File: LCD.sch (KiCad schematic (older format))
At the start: 11 parts

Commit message: Erste fertige Version
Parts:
- R? (x7): value 22 -> 220
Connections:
- net RW renamed R~W~
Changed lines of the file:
@@
 P 4500 3300
 F 0 "R?" V 4450 3150 50  0000 C CNN
-F 1 "22" V 4450 3450 50  0000 C CNN
+F 1 "220" V 4450 3450 50  0000 C CNN
 F 2 "" H 4500 3300 50  0001 C CNN
 F 3 "~" H 4500 3300 50  0001 C CNN
@@
 RS
 Text HLabel 4150 3400 0    50   Input ~ 0
-RW
+R~W~
 Text HLabel 4150 3500 0    50   Input ~ 0
 E
@@
 P 4500 3400
 F 0 "R?" V 4450 3250 50  0000 C CNN
-F 1 "22" V 4450 3550 50  0000 C CNN
+F 1 "220" V 4450 3550 50  0000 C CNN
 F 2 "" H 4500 3400 50  0001 C CNN
 F 3 "~" H 4500 3400 50  0001 C CNN
@@
 P 4500 3500
 F 0 "R?" V 4450 3350 50  0000 C CNN
-F 1 "22" V 4450 3650 50  0000 C CNN
+F 1 "220" V 4450 3650 50  0000 C CNN
 F 2 "" H 4500 3500 50  0001 C CNN
 F 3 "~" H 4500 3500 50  0001 C CNN
@@
 P 4500 4000
 F 0 "R?" V 4450 3850 50  0000 C CNN
-F 1 "22" V 4450 4150 50  0000 C CNN
+F 1 "220" V 4450 4150 50  0000 C CNN
 F 2 "" H 4500 4000 50  0001 C CNN
 F 3 "~" H 4500 4000 50  0001 C CNN
@@
 P 4500 4100
 F 0 "R?" V 4450 3950 50  0000 C CNN
-F 1 "22" V 4450 4250 50  0000 C CNN
+F 1 "220" V 4450 4250 50  0000 C CNN
 F 2 "" H 4500 4100 50  0001 C CNN
 F 3 "~" H 4500 4100 50  0001 C CNN
@@
 P 4500 4200
 F 0 "R?" V 4450 4050 50  0000 C CNN
-F 1 "22" V 4450 4350 50  0000 C CNN
+F 1 "220" V 4450 4350 50  0000 C CNN
 F 2 "" H 4500 4200 50  0001 C CNN
 F 3 "~" H 4500 4200 50  0001 C CNN
@@
 P 4500 4300
 F 0 "R?" V 4450 4150 50  0000 C CNN
-F 1 "22" V 4450 4450 50  0000 C CNN
+F 1 "220" V 4450 4450 50  0000 C CNN
 F 2 "" H 4500 4300 50  0001 C CNN
 F 3 "~" H 4500 4300 50  0001 C CNN

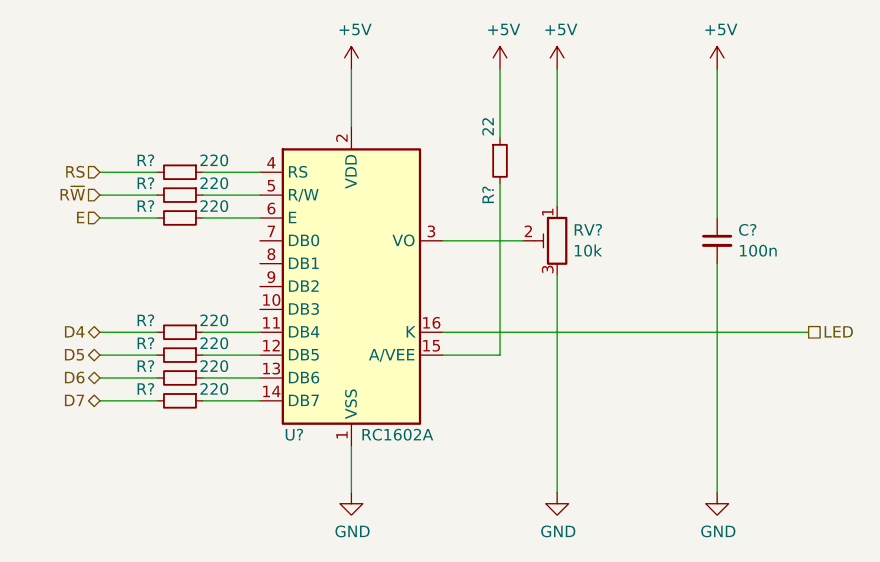
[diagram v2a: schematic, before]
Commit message: Bauteile grob platziert
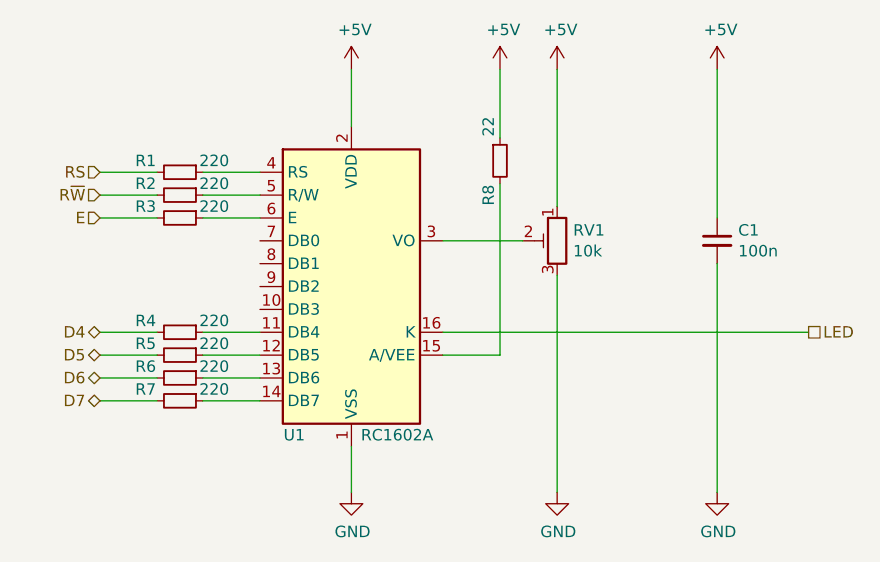
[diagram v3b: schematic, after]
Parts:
- C1: renamed from C?; footprint (none) -> Capacitor_SMD:C_0603_1608Metric_Pad1.05x0.95mm_HandSolder
- R1, R2, R3, R4, R5, R6, R7, R8: renamed from R?; footprint (none) -> Resistor_SMD:R_0603_1608Metric_Pad1.05x0.95mm_HandSolder
- RV1: renamed from RV?; footprint (none) -> Potentiometer_THT:Potentiometer_Bourns_3296P_Horizontal
- U1: renamed from U?; footprint Display:RC1602A -> Display:WC1602A
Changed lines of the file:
@@
 D7
 $Comp
-L Device:R_Small R?
+L Device:R_Small R1
 U 1 1 5EEE17BC
 P 4500 3300
-F 0 "R?" V 4450 3150 50  0000 C CNN
+F 0 "R1" V 4450 3150 50  0000 C CNN
 F 1 "220" V 4450 3450 50  0000 C CNN
-F 2 "" H 4500 3300 50  0001 C CNN
+F 2 "Resistor_SMD:R_0603_1608Metric_Pad1.05x0.95mm_HandSolder" H 4500 3300 50  0001 C CNN
 F 3 "~" H 4500 3300 50  0001 C CNN
 	1    4500 3300
@@
 	4400 3500 4150 3500
 $Comp
-L Device:R_Small R?
+L Device:R_Small R2
 U 1 1 5EEF033B
 P 4500 3400
-F 0 "R?" V 4450 3250 50  0000 C CNN
+F 0 "R2" V 4450 3250 50  0000 C CNN
 F 1 "220" V 4450 3550 50  0000 C CNN
-F 2 "" H 4500 3400 50  0001 C CNN
+F 2 "Resistor_SMD:R_0603_1608Metric_Pad1.05x0.95mm_HandSolder" H 4500 3400 50  0001 C CNN
 F 3 "~" H 4500 3400 50  0001 C CNN
 	1    4500 3400
@@
 $EndComp
 $Comp
-L Device:R_Small R?
+L Device:R_Small R3
 U 1 1 5EEF0596
 P 4500 3500
-F 0 "R?" V 4450 3350 50  0000 C CNN
+F 0 "R3" V 4450 3350 50  0000 C CNN
 F 1 "220" V 4450 3650 50  0000 C CNN
-F 2 "" H 4500 3500 50  0001 C CNN
+F 2 "Resistor_SMD:R_0603_1608Metric_Pad1.05x0.95mm_HandSolder" H 4500 3500 50  0001 C CNN
 F 3 "~" H 4500 3500 50  0001 C CNN
 	1    4500 3500
@@
 $EndComp
 $Comp
-L Device:R_Small R?
+L Device:R_Small R4
 U 1 1 5EEF0900
 P 4500 4000
-F 0 "R?" V 4450 3850 50  0000 C CNN
+F 0 "R4" V 4450 3850 50  0000 C CNN
 F 1 "220" V 4450 4150 50  0000 C CNN
-F 2 "" H 4500 4000 50  0001 C CNN
+F 2 "Resistor_SMD:R_0603_1608Metric_Pad1.05x0.95mm_HandSolder" H 4500 4000 50  0001 C CNN
 F 3 "~" H 4500 4000 50  0001 C CNN
 	1    4500 4000
@@
 $EndComp
 $Comp
-L Device:R_Small R?
+L Device:R_Small R5
 U 1 1 5EEF0B44
 P 4500 4100
-F 0 "R?" V 4450 3950 50  0000 C CNN
+F 0 "R5" V 4450 3950 50  0000 C CNN
 F 1 "220" V 4450 4250 50  0000 C CNN
-F 2 "" H 4500 4100 50  0001 C CNN
+F 2 "Resistor_SMD:R_0603_1608Metric_Pad1.05x0.95mm_HandSolder" H 4500 4100 50  0001 C CNN
 F 3 "~" H 4500 4100 50  0001 C CNN
 	1    4500 4100
@@
 $EndComp
 $Comp
-L Device:R_Small R?
+L Device:R_Small R6
 U 1 1 5EEF0D99
 P 4500 4200
-F 0 "R?" V 4450 4050 50  0000 C CNN
+F 0 "R6" V 4450 4050 50  0000 C CNN
 F 1 "220" V 4450 4350 50  0000 C CNN
-F 2 "" H 4500 4200 50  0001 C CNN
+F 2 "Resistor_SMD:R_0603_1608Metric_Pad1.05x0.95mm_HandSolder" H 4500 4200 50  0001 C CNN
 F 3 "~" H 4500 4200 50  0001 C CNN
 	1    4500 4200
@@
 $EndComp
 $Comp
-L Device:R_Small R?
+L Device:R_Small R7
 U 1 1 5EEF0FCB
 P 4500 4300
-F 0 "R?" V 4450 4150 50  0000 C CNN
+F 0 "R7" V 4450 4150 50  0000 C CNN
 F 1 "220" V 4450 4450 50  0000 C CNN
-F 2 "" H 4500 4300 50  0001 C CNN
+F 2 "Resistor_SMD:R_0603_1608Metric_Pad1.05x0.95mm_HandSolder" H 4500 4300 50  0001 C CNN
 F 3 "~" H 4500 4300 50  0001 C CNN
 	1    4500 4300
@@
 $EndComp
 $Comp
-L Display_Character:RC1602A U?
+L Display_Character:RC1602A U1
 U 1 1 5EEE0198
 P 5250 3800
-F 0 "U?" H 5000 3150 50  0000 C CNN
+F 0 "U1" H 5000 3150 50  0000 C CNN
 F 1 "RC1602A" H 5450 3150 50  0000 C CNN
-F 2 "Display:RC1602A" H 5350 3000 50  0001 C CNN
+F 2 "Display:WC1602A" H 5350 3000 50  0001 C CNN
 F 3 "http://www.raystar-optronics.com/down.php?ProID=18" H 5350 3700 50  0001 C CNN
 	1    5250 3800
@@
 	5650 4000 7250 4000
 $Comp
-L Device:R_Small R?
+L Device:R_Small R8
 U 1 1 5EEF2290
 P 5900 3250
-F 0 "R?" V 5850 3100 50  0000 C CNN
+F 0 "R8" V 5850 3100 50  0000 C CNN
 F 1 "22" V 5850 3400 50  0000 C CNN
-F 2 "" H 5900 3250 50  0001 C CNN
+F 2 "Resistor_SMD:R_0603_1608Metric_Pad1.05x0.95mm_HandSolder" H 5900 3250 50  0001 C CNN
 F 3 "~" H 5900 3250 50  0001 C CNN
 	1    5900 3250
@@
 $EndComp
 $Comp
-L Device:R_POT_TRIM RV?
+L Device:R_POT_TRIM RV1
 U 1 1 5EEF4693
 P 6150 3600
-F 0 "RV?" H 6080 3646 50  0000 R CNN
+F 0 "RV1" H 6080 3646 50  0000 R CNN
 F 1 "10k" H 6080 3555 50  0000 R CNN
-F 2 "" H 6150 3600 50  0001 C CNN
+F 2 "Potentiometer_THT:Potentiometer_Bourns_3296P_Horizontal" H 6150 3600 50  0001 C CNN
 F 3 "~" H 6150 3600 50  0001 C CNN
 	1    6150 3600
@@
 	5650 3600 6000 3600
 $Comp
-L Device:C_Small C?
+L Device:C_Small C1
 U 1 1 5EEF5668
 P 6850 3600
-F 0 "C?" H 6942 3646 50  0000 L CNN
+F 0 "C1" H 6942 3646 50  0000 L CNN
 F 1 "100n" H 6942 3555 50  0000 L CNN
-F 2 "" H 6850 3600 50  0001 C CNN
+F 2 "Capacitor_SMD:C_0603_1608Metric_Pad1.05x0.95mm_HandSolder" H 6850 3600 50  0001 C CNN
 F 3 "~" H 6850 3600 50  0001 C CNN
 	1    6850 3600
@@
 	5900 4100 5650 4100
 $Comp
-L power:+5V #PWR?
+L power:+5V #PWR0101
 U 1 1 5EEF6265
 P 5250 2850
-F 0 "#PWR?" H 5250 2700 50  0001 C CNN
+F 0 "#PWR0101" H 5250 2700 50  0001 C CNN
 F 1 "+5V" H 5265 3023 50  0000 C CNN
 F 2 "" H 5250 2850 50  0001 C CNN
@@
 $EndComp
 $Comp
-L power:+5V #PWR?
+L power:+5V #PWR0102
 U 1 1 5EEF9DD1
 P 5900 2850
-F 0 "#PWR?" H 5900 2700 50  0001 C CNN
+F 0 "#PWR0102" H 5900 2700 50  0001 C CNN
 F 1 "+5V" H 5915 3023 50  0000 C CNN
 F 2 "" H 5900 2850 50  0001 C CNN
@@
 $EndComp
 $Comp
-L power:+5V #PWR?
+L power:+5V #PWR0103
 U 1 1 5EEFA0DF
 P 6150 2850
-F 0 "#PWR?" H 6150 2700 50  0001 C CNN
+F 0 "#PWR0103" H 6150 2700 50  0001 C CNN
 F 1 "+5V" H 6165 3023 50  0000 C CNN
 F 2 "" H 6150 2850 50  0001 C CNN
@@
 $EndComp
 $Comp
-L power:+5V #PWR?
+L power:+5V #PWR0104
 U 1 1 5EEFA5E3
 P 6850 2850
-F 0 "#PWR?" H 6850 2700 50  0001 C CNN
+F 0 "#PWR0104" H 6850 2700 50  0001 C CNN
 F 1 "+5V" H 6865 3023 50  0000 C CNN
 F 2 "" H 6850 2850 50  0001 C CNN
@@
 	6850 2850 6850 3500
 $Comp
-L power:GND #PWR?
+L power:GND #PWR0105
 U 1 1 5EEFD6FC
 P 5250 4700
-F 0 "#PWR?" H 5250 4450 50  0001 C CNN
+F 0 "#PWR0105" H 5250 4450 50  0001 C CNN
 F 1 "GND" H 5255 4527 50  0000 C CNN
 F 2 "" H 5250 4700 50  0001 C CNN
@@
 $EndComp
 $Comp
-L power:GND #PWR?
+L power:GND #PWR0106
 U 1 1 5EEFE087
 P 6150 4700
-F 0 "#PWR?" H 6150 4450 50  0001 C CNN
+F 0 "#PWR0106" H 6150 4450 50  0001 C CNN
 F 1 "GND" H 6155 4527 50  0000 C CNN
 F 2 "" H 6150 4700 50  0001 C CNN
@@
 $EndComp
 $Comp
-L power:GND #PWR?
+L power:GND #PWR0107
 U 1 1 5EEFE62A
 P 6850 4700
-F 0 "#PWR?" H 6850 4450 50  0001 C CNN
+F 0 "#PWR0107" H 6850 4450 50  0001 C CNN
 F 1 "GND" H 6855 4527 50  0000 C CNN
 F 2 "" H 6850 4700 50  0001 C CNN

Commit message: Alle Bauteile platziert
Alle Bauteile sind grob plaziert.
Einige Bauteile sollten noch umplaziert werden (u. a. die Jumper links neben Groov-Con, RGB-LED,).
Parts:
- C1: symbol Device:C_Small -> MCT_Labor_5529-rescue:C_Small-Device
- R1, R2, R3, R4, R5, R6, R7, R8: symbol Device:R_Small -> MCT_Labor_5529-rescue:R_Small-Device
- RV1: symbol Device:R_POT_TRIM -> MCT_Labor_5529-rescue:R_POT_TRIM-Device
- U1: symbol Display_Character:RC1602A -> MCT_Labor_5529-rescue:RC1602A-Display_Character
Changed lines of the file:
@@
 D7
 $Comp
-L Device:R_Small R1
+L MCT_Labor_5529-rescue:R_Small-Device R1
 U 1 1 5EEE17BC
 P 4500 3300
@@
 	4400 3500 4150 3500
 $Comp
-L Device:R_Small R2
+L MCT_Labor_5529-rescue:R_Small-Device R2
 U 1 1 5EEF033B
 P 4500 3400
@@
 $EndComp
 $Comp
-L Device:R_Small R3
+L MCT_Labor_5529-rescue:R_Small-Device R3
 U 1 1 5EEF0596
 P 4500 3500
@@
 $EndComp
 $Comp
-L Device:R_Small R4
+L MCT_Labor_5529-rescue:R_Small-Device R4
 U 1 1 5EEF0900
 P 4500 4000
@@
 $EndComp
 $Comp
-L Device:R_Small R5
+L MCT_Labor_5529-rescue:R_Small-Device R5
 U 1 1 5EEF0B44
 P 4500 4100
@@
 $EndComp
 $Comp
-L Device:R_Small R6
+L MCT_Labor_5529-rescue:R_Small-Device R6
 U 1 1 5EEF0D99
 P 4500 4200
@@
 $EndComp
 $Comp
-L Device:R_Small R7
+L MCT_Labor_5529-rescue:R_Small-Device R7
 U 1 1 5EEF0FCB
 P 4500 4300
@@
 $EndComp
 $Comp
-L Display_Character:RC1602A U1
+L MCT_Labor_5529-rescue:RC1602A-Display_Character U1
 U 1 1 5EEE0198
 P 5250 3800
@@
 	5650 4000 7250 4000
 $Comp
-L Device:R_Small R8
+L MCT_Labor_5529-rescue:R_Small-Device R8
 U 1 1 5EEF2290
 P 5900 3250
@@
 $EndComp
 $Comp
-L Device:R_POT_TRIM RV1
+L MCT_Labor_5529-rescue:R_POT_TRIM-Device RV1
 U 1 1 5EEF4693
 P 6150 3600
@@
 	5650 3600 6000 3600
 $Comp
-L Device:C_Small C1
+L MCT_Labor_5529-rescue:C_Small-Device C1
 U 1 1 5EEF5668
 P 6850 3600
@@
 	5900 4100 5650 4100
 $Comp
-L power:+5V #PWR0101
+L MCT_Labor_5529-rescue:+5V-power #PWR0101
 U 1 1 5EEF6265
 P 5250 2850
@@
 $EndComp
 $Comp
-L power:+5V #PWR0102
+L MCT_Labor_5529-rescue:+5V-power #PWR0102
 U 1 1 5EEF9DD1
 P 5900 2850
@@
 $EndComp
 $Comp
-L power:+5V #PWR0103
+L MCT_Labor_5529-rescue:+5V-power #PWR0103
 U 1 1 5EEFA0DF
 P 6150 2850
@@
 $EndComp
 $Comp
-L power:+5V #PWR0104
+L MCT_Labor_5529-rescue:+5V-power #PWR0104
 U 1 1 5EEFA5E3
 P 6850 2850
@@
 	6850 2850 6850 3500
 $Comp
-L power:GND #PWR0105
+L MCT_Labor_5529-rescue:GND-power #PWR0105
 U 1 1 5EEFD6FC
 P 5250 4700
@@
 $EndComp
 $Comp
-L power:GND #PWR0106
+L MCT_Labor_5529-rescue:GND-power #PWR0106
 U 1 1 5EEFE087
 P 6150 4700
@@
 $EndComp
 $Comp
-L power:GND #PWR0107
+L MCT_Labor_5529-rescue:GND-power #PWR0107
 U 1 1 5EEFE62A
 P 6850 4700

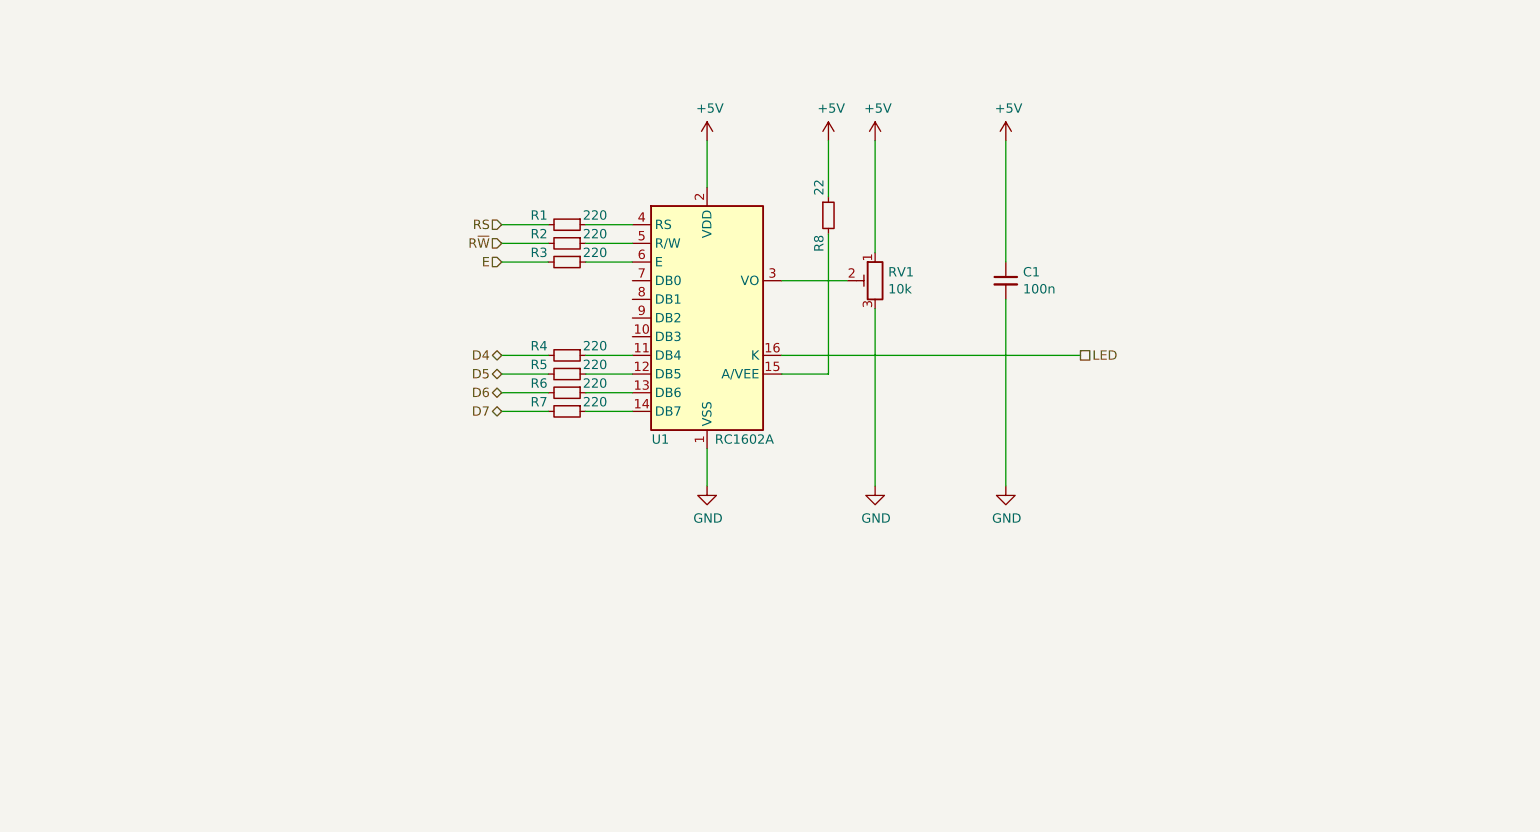
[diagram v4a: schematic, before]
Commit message: Anpassungen am Lüfteranschluss und den LEDs
-Lüfteranschluss verändert
 -> 12V-Versorgung eingefügt
-LED & LCD auf 3,3V umgestellt
 -> Ladungspunpe für neg. Kontrastspannung
-keine 5V Versorgung mehr
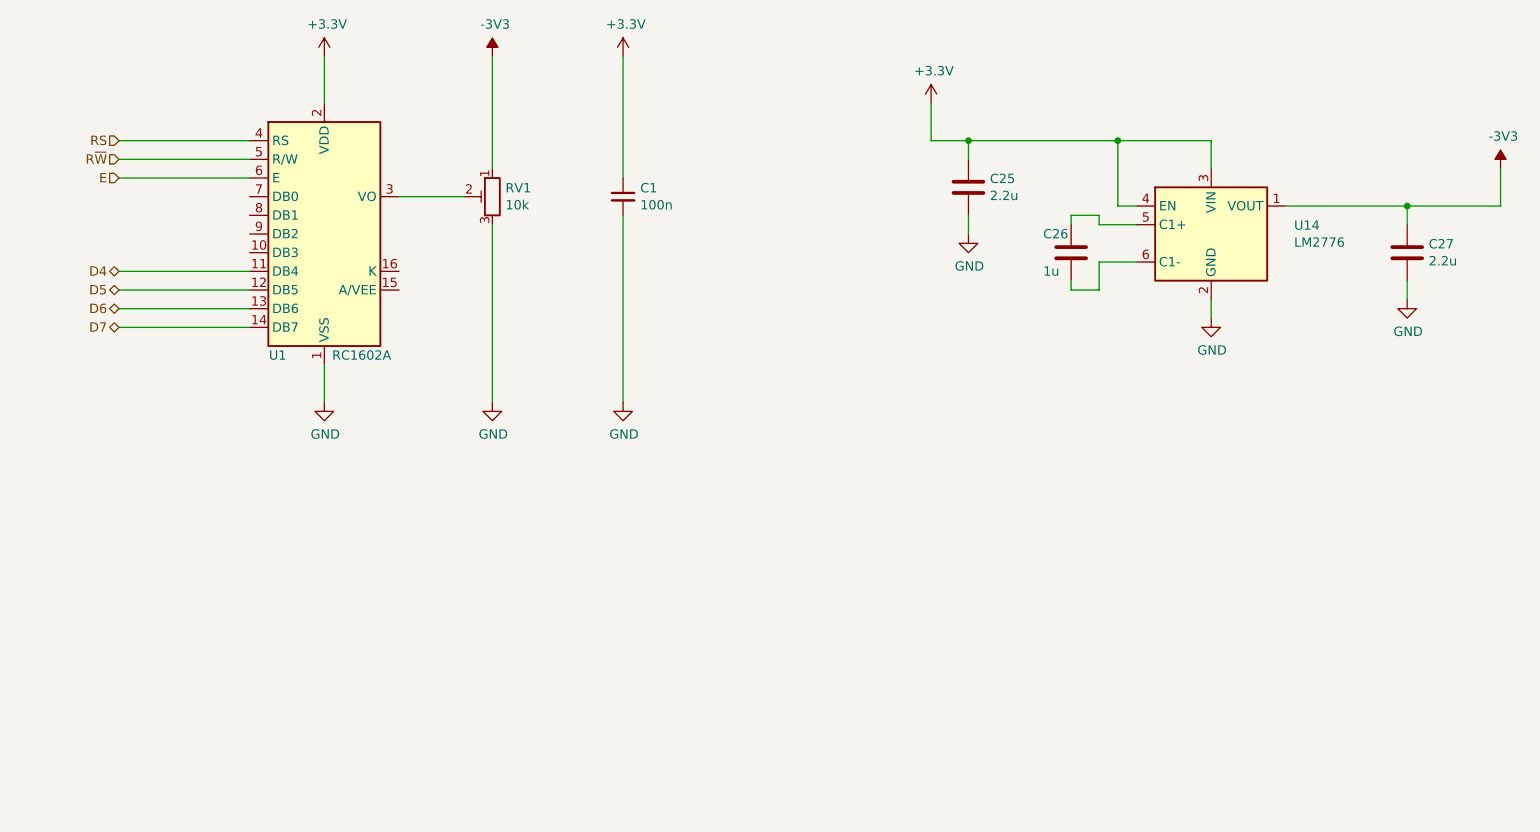
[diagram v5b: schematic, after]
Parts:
- removed R1, R2, R3, R4, R5, R6, R7: 220, Resistor_SMD:R_0603_1608Metric_Pad1.05x0.95mm_HandSolder, symbol MCT_Labor_5529-rescue:R_Small-Device
- removed R8: 22, Resistor_SMD:R_0603_1608Metric_Pad1.05x0.95mm_HandSolder, symbol MCT_Labor_5529-rescue:R_Small-Device
- added C25, C27: 2.2u, Capacitor_SMD:C_0603_1608Metric_Pad1.05x0.95mm_HandSolder, symbol Device:C
- added C26: 1u, Capacitor_SMD:C_0603_1608Metric_Pad1.05x0.95mm_HandSolder, symbol Device:C
- added U14: LM2776, Package_TO_SOT_SMD:SOT-23-6, symbol Regulator_SwitchedCapacitor:LM2776
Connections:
- net D4: now also U1.11 (DB4)
- net D5: now also U1.12 (DB5)
- net D6: now also U1.13 (DB6)
- net D7: now also U1.14 (DB7)
- net E: now also U1.6 (E)
- net GND: now also C25.2, C27.2, U14.2 (GND)
- net RS: now also U1.4 (RS)
- net R~W~: now also U1.5 (R/W)
- net +5V renamed +3V3
- net +3V3: now also C25.1, U14.3 (VIN), U14.4 (EN); no longer RV1.1
- net LED: no longer names the net of U1.16 (K)
- new net: C26.1, U14.5 (C1+)
- new net: C26.2, U14.6 (C1-)
- new net -3V3: C27.1, RV1.1, U14.1 (VOUT)
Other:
- moved on the sheet: C1, RV1, U1

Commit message: Aktuell gefertigte Variante
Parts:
- C25, C27: value 2.2u -> 1µ
- C26: value 1u -> 1µ
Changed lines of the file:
@@
 P 6650 3100
 F 0 "C25" H 6765 3146 50  0000 L CNN
-F 1 "2.2u" H 6765 3055 50  0000 L CNN
+F 1 "1µ" H 6765 3055 50  0000 L CNN
 F 2 "Capacitor_SMD:C_0603_1608Metric_Pad1.05x0.95mm_HandSolder" H 6688 2950 50  0001 C CNN
 F 3 "~" H 6650 3100 50  0001 C CNN
@@
 P 7200 3450
 F 0 "C26" H 7050 3550 50  0000 L CNN
-F 1 "1u" H 7050 3350 50  0000 L CNN
+F 1 "1µ" H 7050 3350 50  0000 L CNN
 F 2 "Capacitor_SMD:C_0603_1608Metric_Pad1.05x0.95mm_HandSolder" H 7238 3300 50  0001 C CNN
 F 3 "~" H 7200 3450 50  0001 C CNN
@@
 P 9000 3450
 F 0 "C27" H 9115 3496 50  0000 L CNN
-F 1 "2.2u" H 9115 3405 50  0000 L CNN
+F 1 "1µ" H 9115 3405 50  0000 L CNN
 F 2 "Capacitor_SMD:C_0603_1608Metric_Pad1.05x0.95mm_HandSolder" H 9038 3300 50  0001 C CNN
 F 3 "~" H 9000 3450 50  0001 C CNN
